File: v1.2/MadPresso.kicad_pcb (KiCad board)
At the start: 2 copper layers, 108 x 57.5 mm, 75 parts, among them J1 Conn_01x07, J2 Conn_01x03, J3 Conn_01x02, J4 Conn_01x04, Q1 BC847, Q2 BSS84, Q3 T835-600B, Q4 2N7002, Q5 T835-600B, Q6 2N7002, Q7 T835-600B, Q8 2N7002, U1 LTV-356T, U2 ADC101C021CIMK, U3 WeMos_D1_mini, U4 MID400, U5 MID400, U6 TLP160G, U7 TLP160G, U8 TLP160G

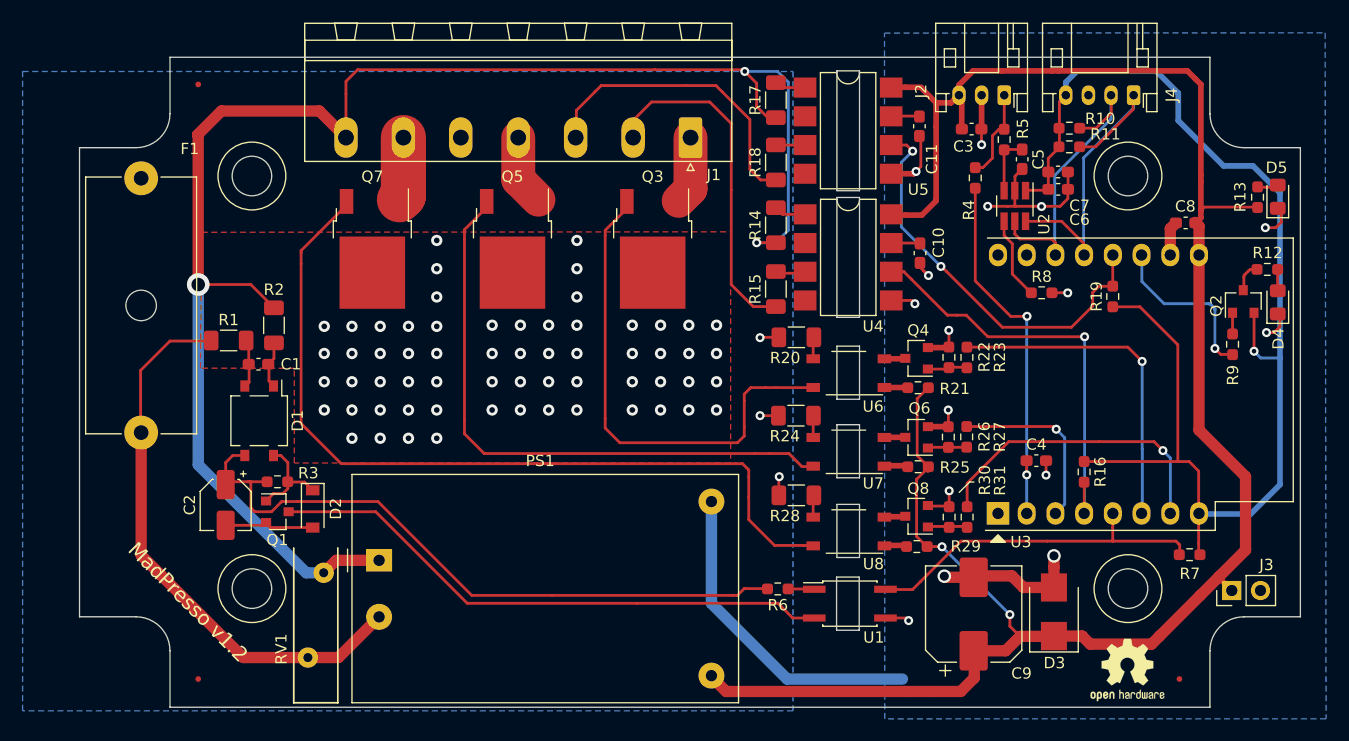
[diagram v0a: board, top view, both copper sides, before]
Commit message: more clearance for LINE and NEUT
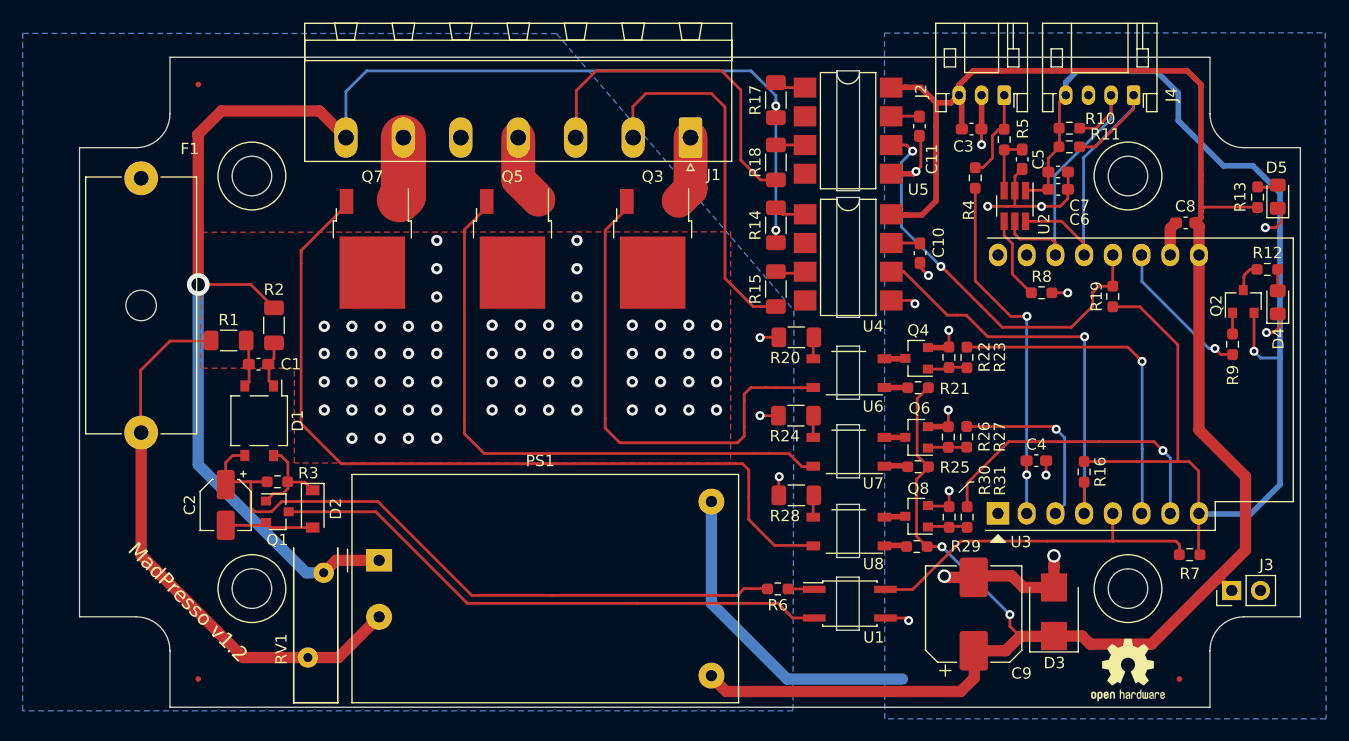
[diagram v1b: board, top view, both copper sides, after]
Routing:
- net NEUT: track 140.9 -> 130.6 mm
- net /STEAM_SW: track 27.0 -> 30.2 mm
- net /LED: track 15.5 -> 13.1 mm
- net /SHOT_SW: track 30.9 -> 32.8 mm
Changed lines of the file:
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@@
   (title_block
     (title "MadPresso")
-    (date "2020-11-26")
+    (date "2020-12-05")
     (rev "1.2")
   )
@@
   )
   (footprint "Symbol:OSHW-Logo2_7.3x6mm_SilkScreen" (layer "F.Cu")
-    (at 92.7 54.2)
+    (at 92.75 54.2)
     (descr "Open Source Hardware Symbol")
     (tags "Logo Symbol OSHW")
@@
   (segment (start 10.5 6.9) (end 10.5 20.1) (width 1) (layer "F.Cu") (net 10))
   (segment (start 15.15 20.1) (end 17.15 22.1) (width 0.25) (layer "F.Cu") (net 10))
-  (segment (start 23.57 2.13) (end 24.6 1.1) (width 0.25) (layer "F.Cu") (net 10))
+  (segment (start 61.6 4.3) (end 61.6 5.3) (width 0.25) (layer "F.Cu") (net 10))
   (segment (start 21.22 4.75) (end 12.55 4.75) (width 1) (layer "F.Cu") (net 10))
-  (segment (start 50.9 1.1) (end 58.7 1.1) (width 0.25) (layer "F.Cu") (net 10))
-  (segment (start 24.6 1.1) (end 50.9 1.1) (width 0.25) (layer "F.Cu") (net 10))
-  (segment (start 59.9 4.35) (end 60.9 5.35) (width 0.25) (layer "F.Cu") (net 10))
+  (segment (start 61.6 15.3) (end 61.6 16.5) (width 0.25) (layer "F.Cu") (net 10))
   (segment (start 26.5 44.5) (end 22.7 44.5) (width 1) (layer "F.Cu") (net 10))
-  (segment (start 23.57 7.1) (end 23.57 3.23) (width 0.25) (layer "F.Cu") (net 10))
-  (segment (start 59.9 2.3) (end 59.9 4.35) (width 0.25) (layer "F.Cu") (net 10))
   (segment (start 12.55 4.75) (end 10.45 6.85) (width 1) (layer "F.Cu") (net 10))
-  (segment (start 23.57 3.23) (end 23.57 2.13) (width 0.25) (layer "F.Cu") (net 10))
-  (segment (start 61.6 16.4) (end 59.9 16.4) (width 0.25) (layer "F.Cu") (net 10))
   (segment (start 23.57 7.1) (end 21.22 4.75) (width 1) (layer "F.Cu") (net 10))
-  (segment (start 58.7 1.1) (end 59.9 2.3) (width 0.25) (layer "F.Cu") (net 10))
-  (segment (start 60.9 5.35) (end 61.6 5.35) (width 0.25) (layer "F.Cu") (net 10))
   (segment (start 22.7 44.5) (end 21.5 45.7) (width 1) (layer "F.Cu") (net 10))
   (segment (start 10.45 6.85) (end 10.5 6.9) (width 1) (layer "F.Cu") (net 10))
   (via (at 10.5 20.1) (size 2) (drill 1.2) (layers "F.Cu" "B.Cu") (remove_unused_layers) (keep_end_layers) (net 10))
-  (via (at 59.9 16.4) (size 0.8) (drill 0.4) (layers "F.Cu" "B.Cu") (remove_unused_layers) (keep_end_layers) (net 10))
-  (via (at 58.85 1.25) (size 0.8) (drill 0.4) (layers "F.Cu" "B.Cu") (remove_unused_layers) (keep_end_layers) (net 10))
-  (segment (start 58.85 1.25) (end 61.75 1.25) (width 0.25) (layer "B.Cu") (net 10))
+  (via (at 61.6 4.3) (size 0.8) (drill 0.4) (layers "F.Cu" "B.Cu") (net 10))
+  (via (at 61.6 15.3) (size 0.8) (drill 0.4) (layers "F.Cu" "B.Cu") (net 10))
+  (segment (start 23.57 3.03) (end 25.4 1.2) (width 0.25) (layer "B.Cu") (net 10))
   (segment (start 10.5 36.05) (end 10.5 20.1) (width 1) (layer "B.Cu") (net 10))
+  (segment (start 23.57 7.1) (end 23.57 3.03) (width 0.25) (layer "B.Cu") (net 10))
   (segment (start 10.5 36.05) (end 20.05 45.6) (width 1) (layer "B.Cu") (net 10))
+  (segment (start 61.6 3.8) (end 61.6 4.3) (width 0.25) (layer "B.Cu") (net 10))
   (segment (start 21.6 45.6) (end 20.05 45.6) (width 1) (layer "B.Cu") (net 10))
-  (segment (start 61.6 16.4) (end 59.9 16.4) (width 0.25) (layer "B.Cu") (net 10))
-  (segment (start 61.75 1.25) (end 62.7 2.2) (width 0.25) (layer "B.Cu") (net 10))
-  (segment (start 62.7 2.2) (end 62.7 15.3) (width 0.25) (layer "B.Cu") (net 10))
-  (segment (start 62.7 15.3) (end 61.6 16.4) (width 0.25) (layer "B.Cu") (net 10))
+  (segment (start 25.4 1.2) (end 59.4 1.2) (width 0.25) (layer "B.Cu") (net 10))
+  (segment (start 61.6 3.4) (end 61.6 3.8) (width 0.25) (layer "B.Cu") (net 10))
+  (segment (start 59.4 1.2) (end 61.6 3.4) (width 0.25) (layer "B.Cu") (net 10))
+  (segment (start 61.6 3.8) (end 61.6 15.3) (width 0.25) (layer "B.Cu") (net 10))
   (segment (start 74.05 37.75) (end 74.05 37.33) (width 0.25) (layer "F.Cu") (net 11))
   (segment (start 73.11 13.96) (end 74.51 13.96) (width 0.5) (layer "F.Cu") (net 11))
@@
   (segment (start 91.4 41.6) (end 91.4 40.2) (width 0.25) (layer "F.Cu") (net 15))
   (segment (start 73.695 47.08) (end 71.095 47.08) (width 0.25) (layer "F.Cu") (net 15))
-  (segment (start 55.75 3.95) (end 57.65 5.85) (width 0.25) (layer "F.Cu") (net 16))
-  (segment (start 59.6 22.05) (end 59.25 21.7) (width 0.25) (layer "F.Cu") (net 16))
-  (segment (start 50.6 3.95) (end 48.95 5.6) (width 0.25) (layer "F.Cu") (net 16))
-  (segment (start 61.6 22.05) (end 59.6 22.05) (width 0.25) (layer "F.Cu") (net 16))
-  (segment (start 57.65 20.1) (end 59.25 21.7) (width 0.25) (layer "F.Cu") (net 16))
-  (segment (start 48.95 5.6) (end 48.95 7.35) (width 0.25) (layer "F.Cu") (net 16))
-  (segment (start 50.6 3.95) (end 55.75 3.95) (width 0.25) (layer "F.Cu") (net 16))
-  (segment (start 57.65 5.85) (end 57.65 11.75) (width 0.25) (layer "F.Cu") (net 16))
-  (segment (start 57.65 11.75) (end 57.65 20.1) (width 0.25) (layer "F.Cu") (net 16))
+  (segment (start 57.1 4.4) (end 57.1 19.55) (width 0.25) (layer "F.Cu") (net 16))
+  (segment (start 48.95 7.35) (end 48.95 4.35) (width 0.25) (layer "F.Cu") (net 16))
+  (segment (start 50.1 3.2) (end 55.9 3.2) (width 0.25) (layer "F.Cu") (net 16))
+  (segment (start 55.9 3.2) (end 57.1 4.4) (width 0.25) (layer "F.Cu") (net 16))
+  (segment (start 57.1 19.55) (end 59.6 22.05) (width 0.25) (layer "F.Cu") (net 16))
+  (segment (start 59.6 22.05) (end 61.6 22.05) (width 0.25) (layer "F.Cu") (net 16))
+  (segment (start 48.95 4.35) (end 50.1 3.2) (width 0.25) (layer "F.Cu") (net 16))
   (segment (start 38.81 10.81) (end 40.6 12.6) (width 3) (layer "F.Cu") (net 17))
   (segment (start 38.81 7.1) (end 38.81 10.81) (width 3) (layer "F.Cu") (net 17))
@@
   (segment (start 93.25 4.47) (end 88.82 8.9) (width 0.25) (layer "B.Cu") (net 20))
   (segment (start 88.82 8.9) (end 88.82 17.63) (width 0.25) (layer "B.Cu") (net 20))
-  (segment (start 61.6 10.85) (end 60.25 10.85) (width 0.25) (layer "F.Cu") (net 21))
-  (segment (start 59.3 9.9) (end 59.3 5.5) (width 0.25) (layer "F.Cu") (net 21))
-  (segment (start 43.95 4.7) (end 43.95 7.15) (width 0.25) (layer "F.Cu") (net 21))
-  (segment (start 45.6 3.05) (end 46.15 2.5) (width 0.25) (layer "F.Cu") (net 21))
-  (segment (start 45.6 3.05) (end 43.95 4.7) (width 0.25) (layer "F.Cu") (net 21))
-  (segment (start 56.3 2.5) (end 56.85 3.05) (width 0.25) (layer "F.Cu") (net 21))
-  (segment (start 53.6 2.5) (end 56.3 2.5) (width 0.25) (layer "F.Cu") (net 21))
-  (segment (start 60.25 10.85) (end 59.3 9.9) (width 0.25) (layer "F.Cu") (net 21))
-  (segment (start 46.15 2.5) (end 53.6 2.5) (width 0.25) (layer "F.Cu") (net 21))
-  (segment (start 59.3 5.5) (end 56.85 3.05) (width 0.25) (layer "F.Cu") (net 21))
+  (segment (start 60.25 10.85) (end 61.6 10.85) (width 0.25) (layer "F.Cu") (net 21))
+  (segment (start 58.5 2.9) (end 58.5 9.1) (width 0.25) (layer "F.Cu") (net 21))
+  (segment (start 56.8 1.2) (end 58.5 2.9) (width 0.25) (layer "F.Cu") (net 21))
+  (segment (start 43.95 2.95) (end 45.7 1.2) (width 0.25) (layer "F.Cu") (net 21))
+  (segment (start 43.95 7.15) (end 43.95 2.95) (width 0.25) (layer "F.Cu") (net 21))
+  (segment (start 58.5 9.1) (end 60.25 10.85) (width 0.25) (layer "F.Cu") (net 21))
+  (segment (start 45.7 1.2) (end 56.8 1.2) (width 0.25) (layer "F.Cu") (net 21))
   (segment (start 73.16 7.76) (end 73.7 8.3) (width 0.25) (layer "F.Cu") (net 22))
   (segment (start 87.75 23.88) (end 89.63 22) (width 0.25) (layer "F.Cu") (net 22))
@@
   (segment (start 101.94 26.2825) (end 101.96 26.2625) (width 0.25) (layer "F.Cu") (net 34))
   (via (at 100.44 25.7625) (size 0.8) (drill 0.4) (layers "F.Cu" "B.Cu") (remove_unused_layers) (keep_end_layers) (net 34))
-  (segment (start 100.44 22.243479) (end 100.44141 22.242171) (width 0.25) (layer "B.Cu") (net 34))
-  (segment (start 100.117158 21.917157) (end 100.431599 22.231598) (width 0.25) (layer "B.Cu") (net 34))
   (segment (start 95.93 21.78) (end 93.98 19.83) (width 0.25) (layer "B.Cu") (net 34))
-  (segment (start 95.958284 21.8) (end 99.983268 21.8) (width 0.25) (layer "B.Cu") (net 34))
   (segment (start 95.93 21.78) (end 95.944142 21.794142) (width 0.25) (layer "B.Cu") (net 34))
-  (segment (start 100.44 25.7625) (end 100.44 22.243479) (width 0.25) (layer "B.Cu") (net 34))
   (segment (start 93.98 19.83) (end 93.98 17.43) (width 0.25) (layer "B.Cu") (net 34))
-  (arc (start 99.834315 21.8) (mid 99.987388 21.830448) (end 100.117158 21.917157) (width 0.25) (layer "B.Cu") (net 34))
+  (segment (start 99.9125 25.7625) (end 100.44 25.7625) (width 0.25) (layer "B.Cu") (net 34))
+  (segment (start 95.944142 21.794142) (end 99.9125 25.7625) (width 0.25) (layer "B.Cu") (net 34))
   (arc (start 95.944142 21.794142) (mid 95.95063 21.798477) (end 95.958284 21.8) (width 0.25) (layer "B.Cu") (net 34))
-  (arc (start 100.345442 22.145441) (mid 100.415425 22.250178) (end 100.44 22.373724) (width 0.25) (layer "B.Cu") (net 34))
   (segment (start 83.7775 35.68) (end 83.7775 36.9275) (width 0.25) (layer "F.Cu") (net 35))
   (segment (start 79.24 11.585) (end 79.24 19.78) (width 0.25) (layer "F.Cu") (net 35))
@@
   )
   (zone (net 6) (net_name "LINE") (layer "B.Cu") (hatch edge 0.508)
-    (connect_pads (clearance 2))
+    (connect_pads (clearance 3))
     (min_thickness 0.254) (filled_areas_thickness no)
-    (fill yes (thermal_gap 0.508) (thermal_bridge_width 2))
+    (fill yes (thermal_gap 0.508) (thermal_bridge_width 4))
     (polygon
       (pts
+        (xy 63.2 22.4)
         (xy 63.11514 57.81)
         (xy -5.035838 57.81)
-        (xy -5.035838 1.25252)
-        (xy 63.11514 1.25252)
+        (xy -5.025389 -2.115438)
+        (xy 42.2 -2.1)
       )
     )

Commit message: More updates
* make pump triac switch NEUT, not LINE
* move ADC a bit
* improve clearance
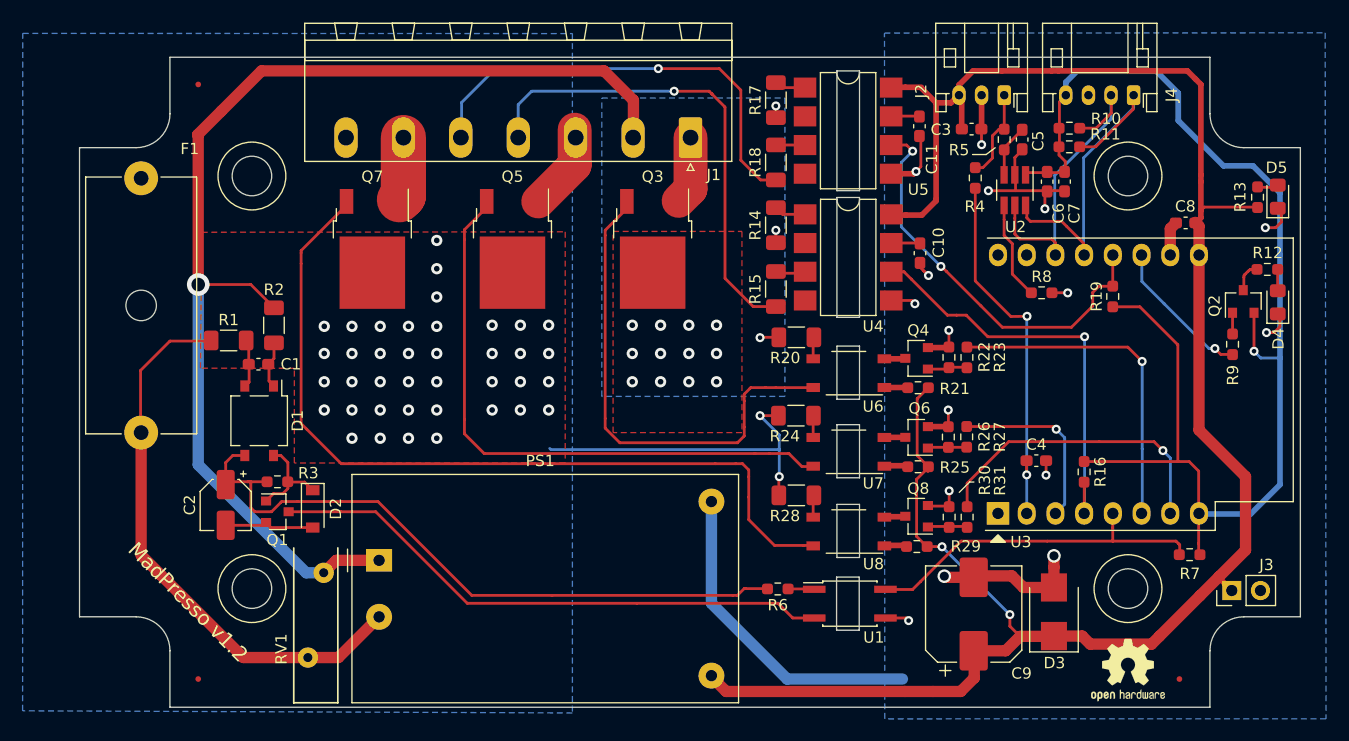
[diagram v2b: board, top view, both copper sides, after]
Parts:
- C10, C11: value DNP -> 1nF
- C5: value 470pF -> 100nF
- moved C5 1.74 mm to (83.4, 7.28)
- moved U2 1.40 mm to (82.7, 11.8)
- moved C6 1.19 mm to (85.6, 11.0), turned to -90 degrees
- moved C7 1.02 mm to (87.1, 11.0), turned to -90 degrees
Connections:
- J1 pad 2: /SHOT_SW -> NEUT
- J1 pad 3: /STEAM_SW -> /VALVE
- J1 pad 4: /VALVE -> /SHOT_SW
- J1 pad 5: LINE -> /STEAM_SW
- J1 pad 7: NEUT -> LINE
- Q3 pad 2: LINE -> NEUT
- R20 pad 2: LINE -> NEUT
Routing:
- net LINE: track 5.03 -> 29.8 mm, vias 65 -> 41
- net NEUT: track 130.6 -> 106.7 mm, vias 3 -> 16
- net /SHOT_SW: track 32.8 -> 43.1 mm, vias 0 -> 1
- net /STEAM_SW: track 30.2 -> 40.0 mm, vias 0 -> 1
- net /VALVE: track 6.24 -> 7.68 mm
- net Net-(R8-Pad1): track 7.29 -> 8.69 mm
- net /SCL: track 27.4 -> 28.8 mm
- net /SDA: track 30.5 -> 31.7 mm
- net GND: track 92.8 -> 92.2 mm
- added copper zone on B.Cu, net NEUT
- added copper zone on F.Cu, net NEUT

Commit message: Improve clearance
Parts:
- moved Q7 2.43 mm to (26.8, 19.2)
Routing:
- net NEUT: track 106.7 -> 113.1 mm, vias 16 -> 15
- net LINE: track 29.8 -> 35.7 mm, vias 41 -> 28
- net Net-(Q3-Pad3): track 44.0 -> 39.0 mm
- net Net-(Q7-Pad3): track 73.7 -> 74.9 mm
- net /HEATER: track 5.64 -> 6.65 mm
- net /SHOT_SW: track 43.1 -> 42.4 mm

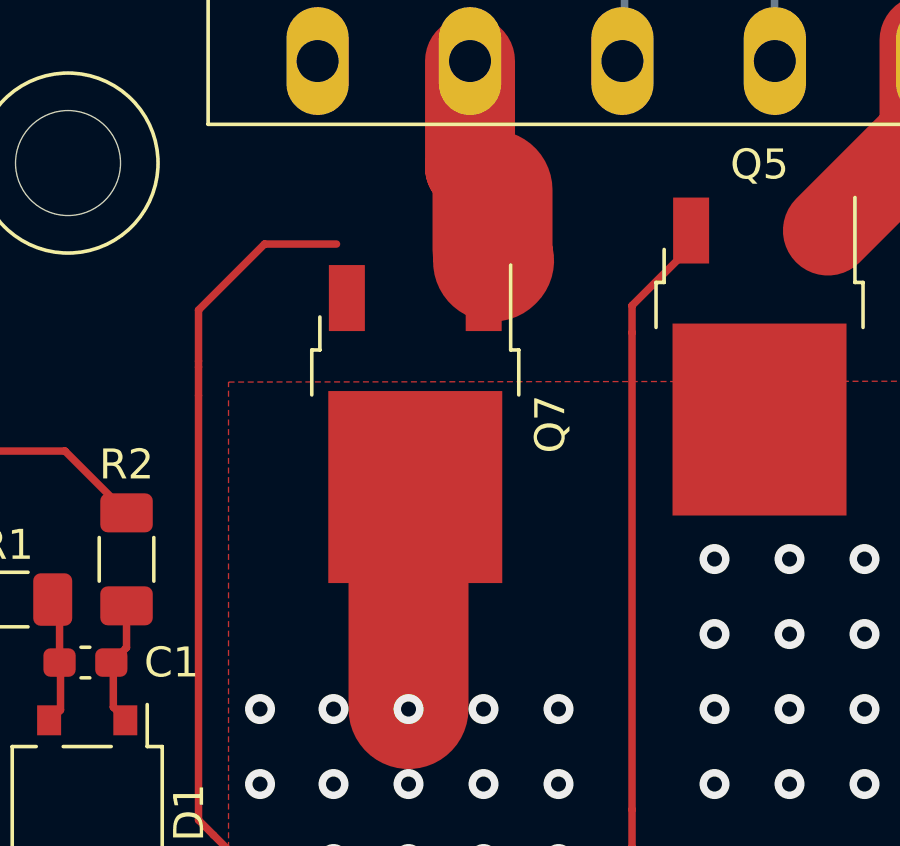
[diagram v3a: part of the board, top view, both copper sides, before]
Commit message: change q7 to TO263 (D2PAK) package
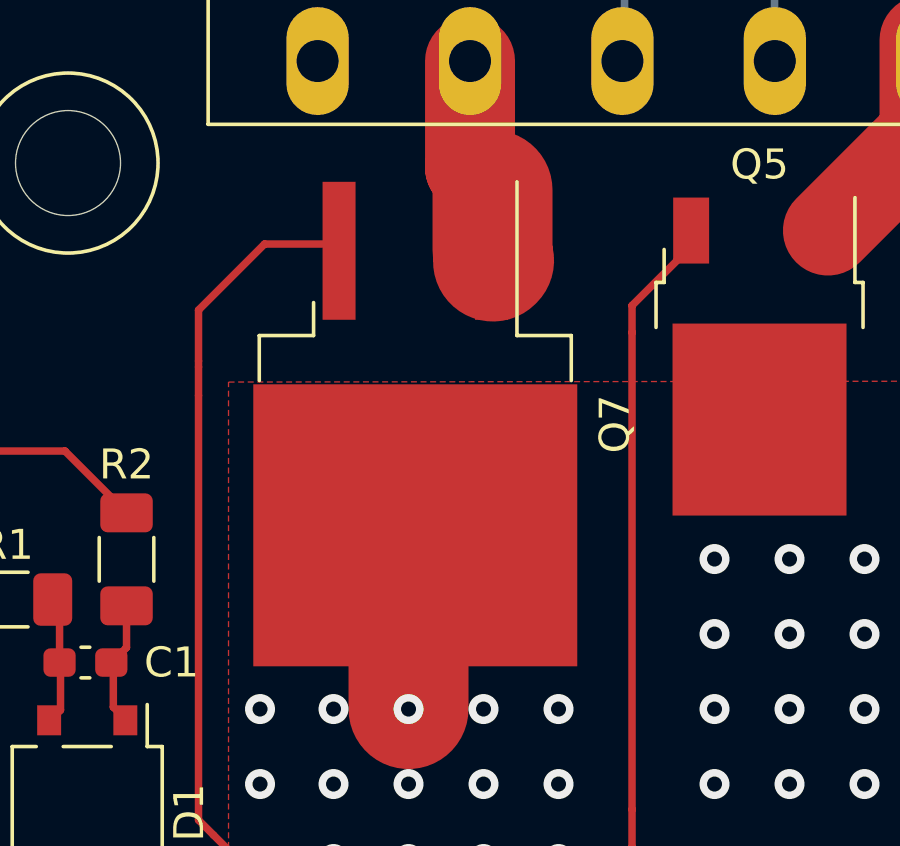
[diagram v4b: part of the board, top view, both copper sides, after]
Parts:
- Q7: footprint Package_TO_SOT_SMD:TO-252-2 -> Package_TO_SOT_SMD:TO-263-2
